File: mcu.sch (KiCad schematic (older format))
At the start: 45 parts

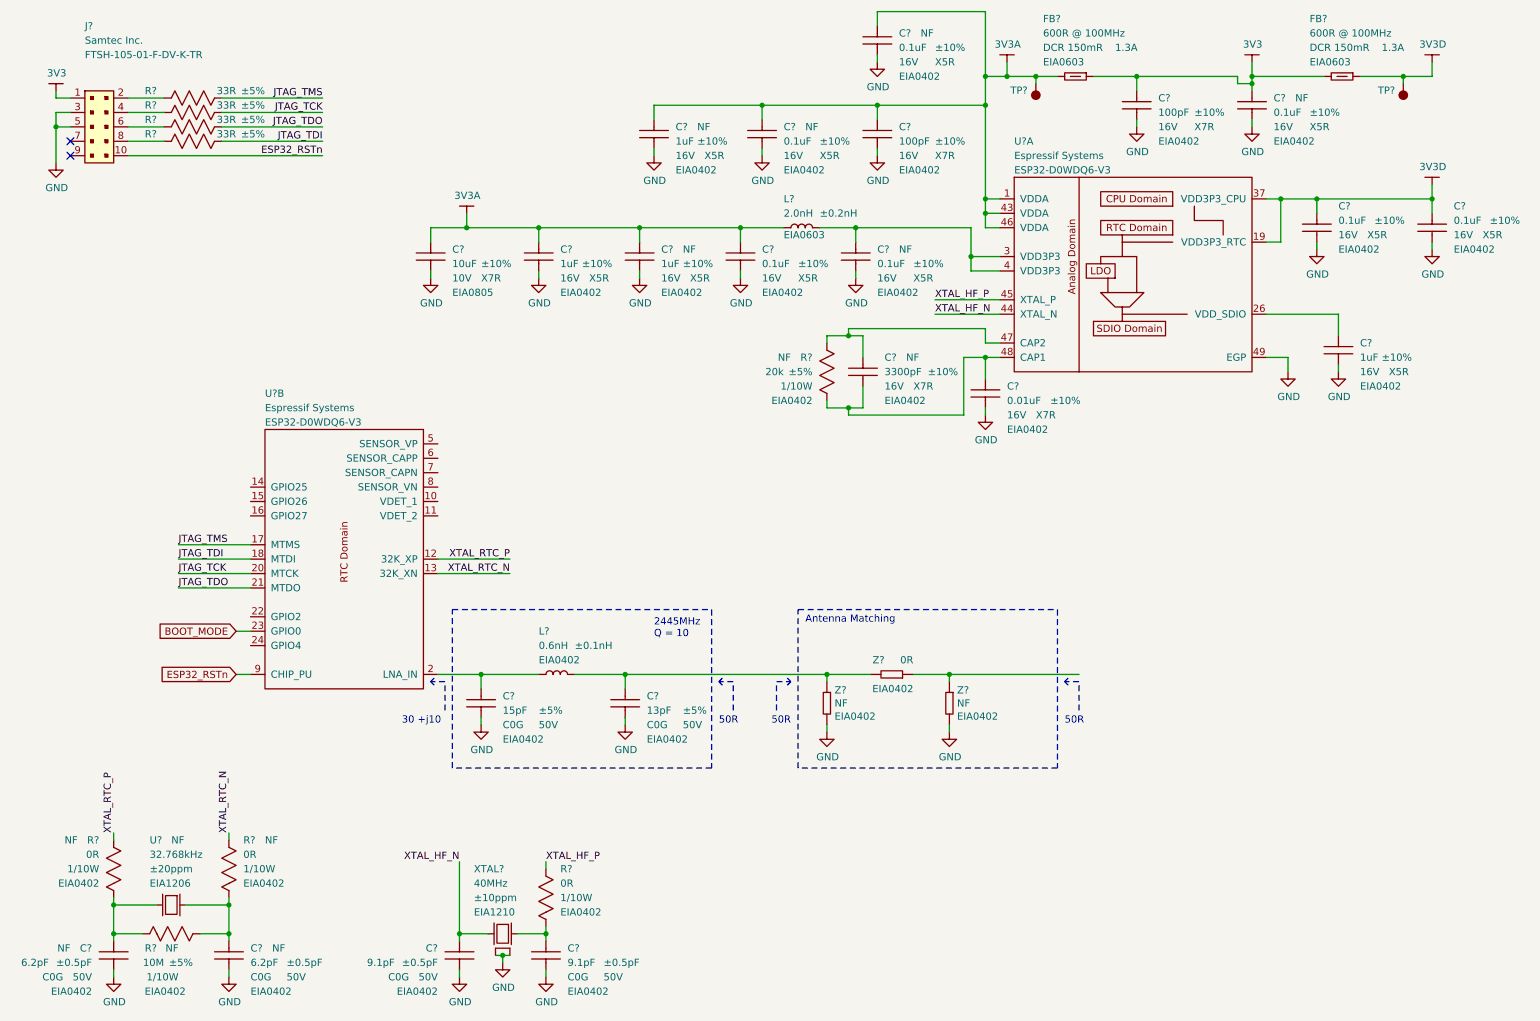
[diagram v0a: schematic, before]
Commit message: Bring out on headers all unused ESP32 pins.
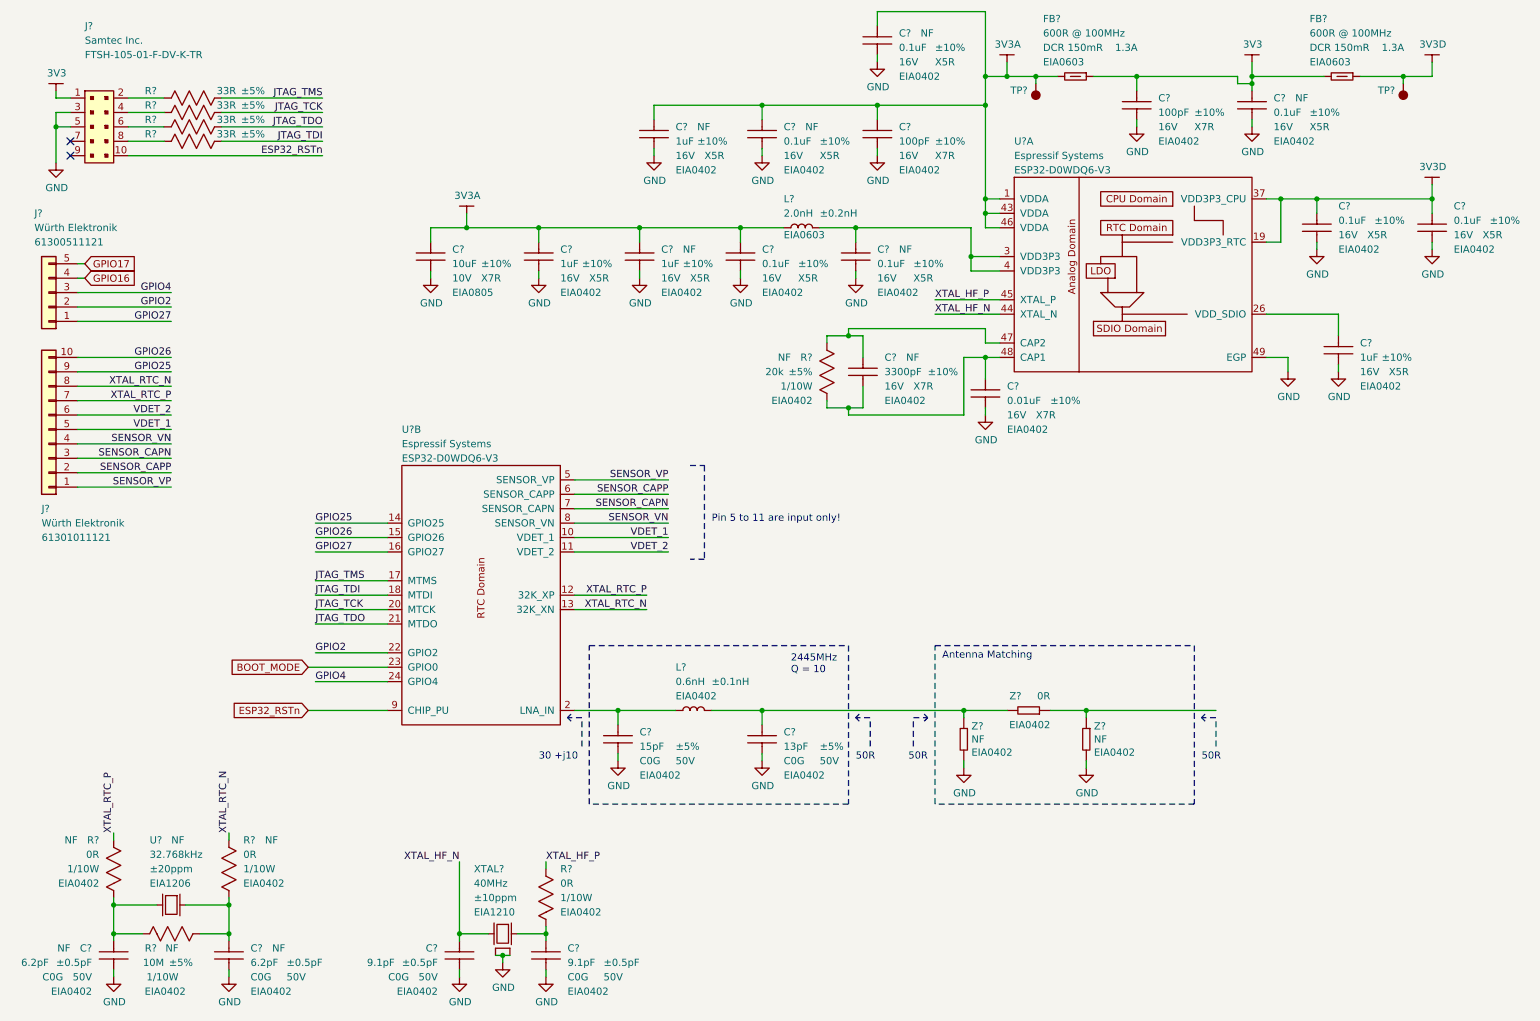
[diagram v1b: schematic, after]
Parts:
- added J?: WE-61301011121, footprints:WE-61301011121_HDRV10W64P254_10X1_2540X254X884N, symbol gz_Rectangular-Connectors-Headers-Male-Pins:WE-61301011121
- added J?: WE-61300511121, footprints:WE-61300511121_HDRV5W79P254_5X1_1270X254H854, symbol gz_Rectangular-Connectors-Headers-Male-Pins:WE-61300511121
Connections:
- net XTAL_RTC_N: now also J?.8 (Pin_8)
- net XTAL_RTC_P: now also J?.7 (Pin_7)
- net VDET_1: now reaches U?.10 (VDET_1)
- net VDET_1: now also J?.5 (Pin_5)
- net VDET_2: now reaches U?.11 (VDET_2)
- net VDET_2: now also J?.6 (Pin_6)
- net GPIO25: now reaches U?.14 (GPIO25)
- net GPIO25: now also J?.9 (Pin_9)
- net GPIO26: now reaches U?.15 (GPIO26)
- net GPIO26: now also J?.10 (Pin_10)
- net GPIO27: now reaches U?.16 (GPIO27)
- net GPIO27: now also J?.1 (Pin_1)
- net GPIO2: now reaches U?.22 (GPIO2)
- net GPIO2: now also J?.2 (Pin_2)
- net GPIO4: now reaches U?.24 (GPIO4)
- net GPIO4: now also J?.3 (Pin_3)
- net SENSOR_VP: now reaches U?.5 (SENSOR_VP)
- net SENSOR_VP: now also J?.1 (Pin_1)
- net SENSOR_CAPP: now reaches U?.6 (SENSOR_CAPP)
- net SENSOR_CAPP: now also J?.2 (Pin_2)
- net SENSOR_CAPN: now reaches U?.7 (SENSOR_CAPN)
- net SENSOR_CAPN: now also J?.3 (Pin_3)
- net SENSOR_VN: now reaches U?.8 (SENSOR_VN)
- net SENSOR_VN: now also J?.4 (Pin_4)
- new net GPIO16: J?.4 (Pin_4)
- new net GPIO17: J?.5 (Pin_5)
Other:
- note added: "Pin 5 to 11 are input only!"
- moved on the sheet: C?, L?, U?B, Z?

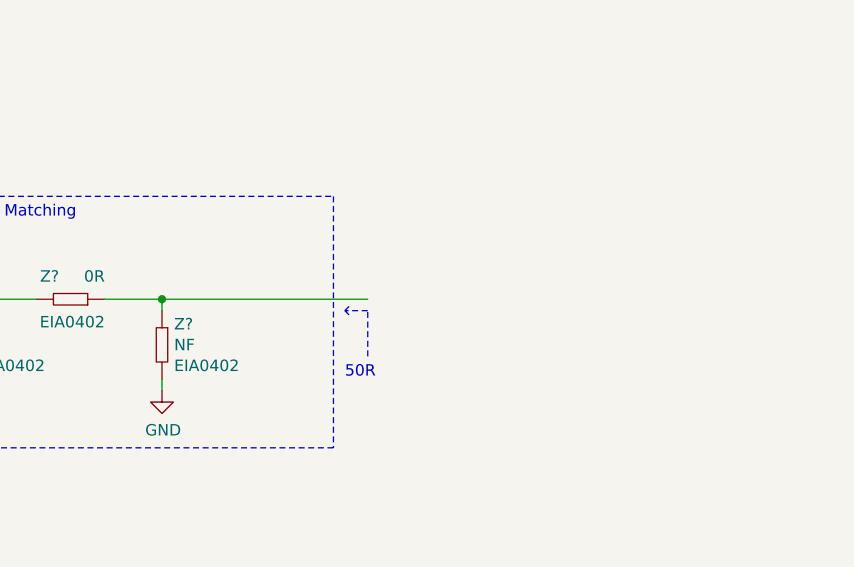
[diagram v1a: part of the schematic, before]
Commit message: Add antenna.
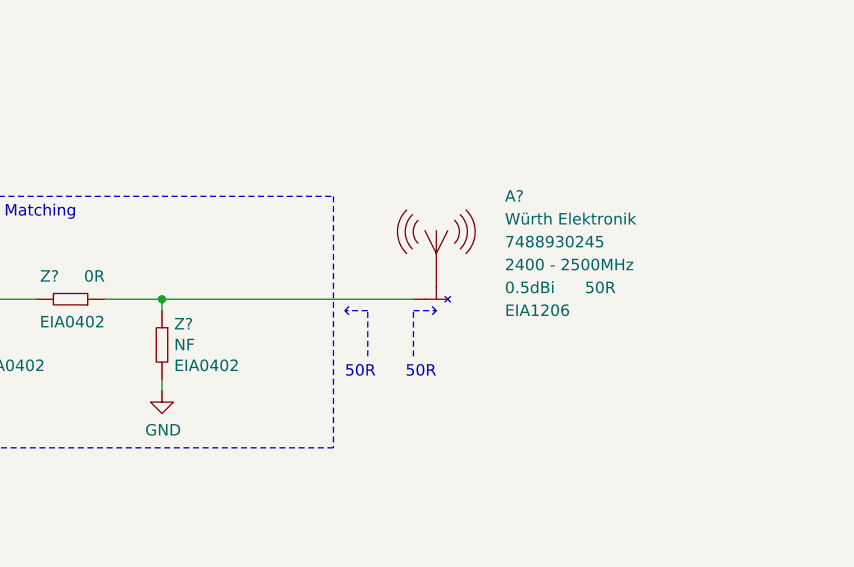
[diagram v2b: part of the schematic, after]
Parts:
- added A?: WE-7488930245, footprints:WE-7488930245_ANTC320X160X140L50N, symbol gz_RF-Antennas:WE-7488930245
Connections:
- net at Z?.1, Z?.1: now also A?.1
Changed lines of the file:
@@
 Wire Notes Line style solid
 	8900 5550 8925 5575
-Wire Wire Line
-	8100 5500 9000 5500
 Connection ~ 8100 5500
 Wire Wire Line
@@
 	1    0    0    1
 $EndComp
+$Comp
+L gz_RF-Antennas:WE-7488930245 A?
+U 1 1 60620A37
+P 9200 5500
+F 0 "A?" H 9600 5950 50  0000 L CNN
+F 1 "WE-7488930245" H 10000 6400 50  0001 L CNN
+F 2 "footprints:WE-7488930245_ANTC320X160X140L50N" H 10000 6500 50  0001 L CNN
+F 3 "${DATASHEETS}/WE-7488930245.pdf" H 10250 5650 50  0001 L CNN
+F 4 "Digikey" H 10000 6300 50  0001 L CNN "Vendor"
+F 5 "732-1843-1-ND" H 10350 6300 50  0001 L CNN "Vendor_PN"
+F 6 "Würth Elektronik" H 9600 5850 50  0000 L CNN "Manufacturer"
+F 7 "7488930245" H 9600 5750 50  0000 L CNN "MPN"
+F 8 "RF/IF and RFID" H 10000 6200 50  0001 L CNN "Category"
+F 9 "RF Antennas" H 10000 6100 50  0001 L CNN "Family"
+F 10 "2400 - 2500MHz" H 9600 5650 50  0000 L CNN "Frequency"
+F 11 "0.5dBi" H 9600 5550 50  0000 L CNN "Peak Gain"
+F 12 "50R" H 9950 5550 50  0000 L CNN "Impedance"
+F 13 "Yes" H 9600 5350 50  0001 L CNN "Fit"
+F 14 "EIA1206" H 9600 5450 50  0000 L CNN "Package"
+	1    9200 5500
+	1    0    0    -1
+$EndComp
+Wire Wire Line
+	8100 5500 9200 5500
+Text Notes 9300 5850 2    50   ~ 0
+50R
+Wire Notes Line style solid
+	9200 5750 9200 5550
+Wire Notes Line style solid
+	9200 5550 9300 5550
+Wire Notes Line style solid
+	9300 5550 9275 5525
+Wire Notes Line style solid
+	9300 5550 9275 5575
 $EndSCHEMATC

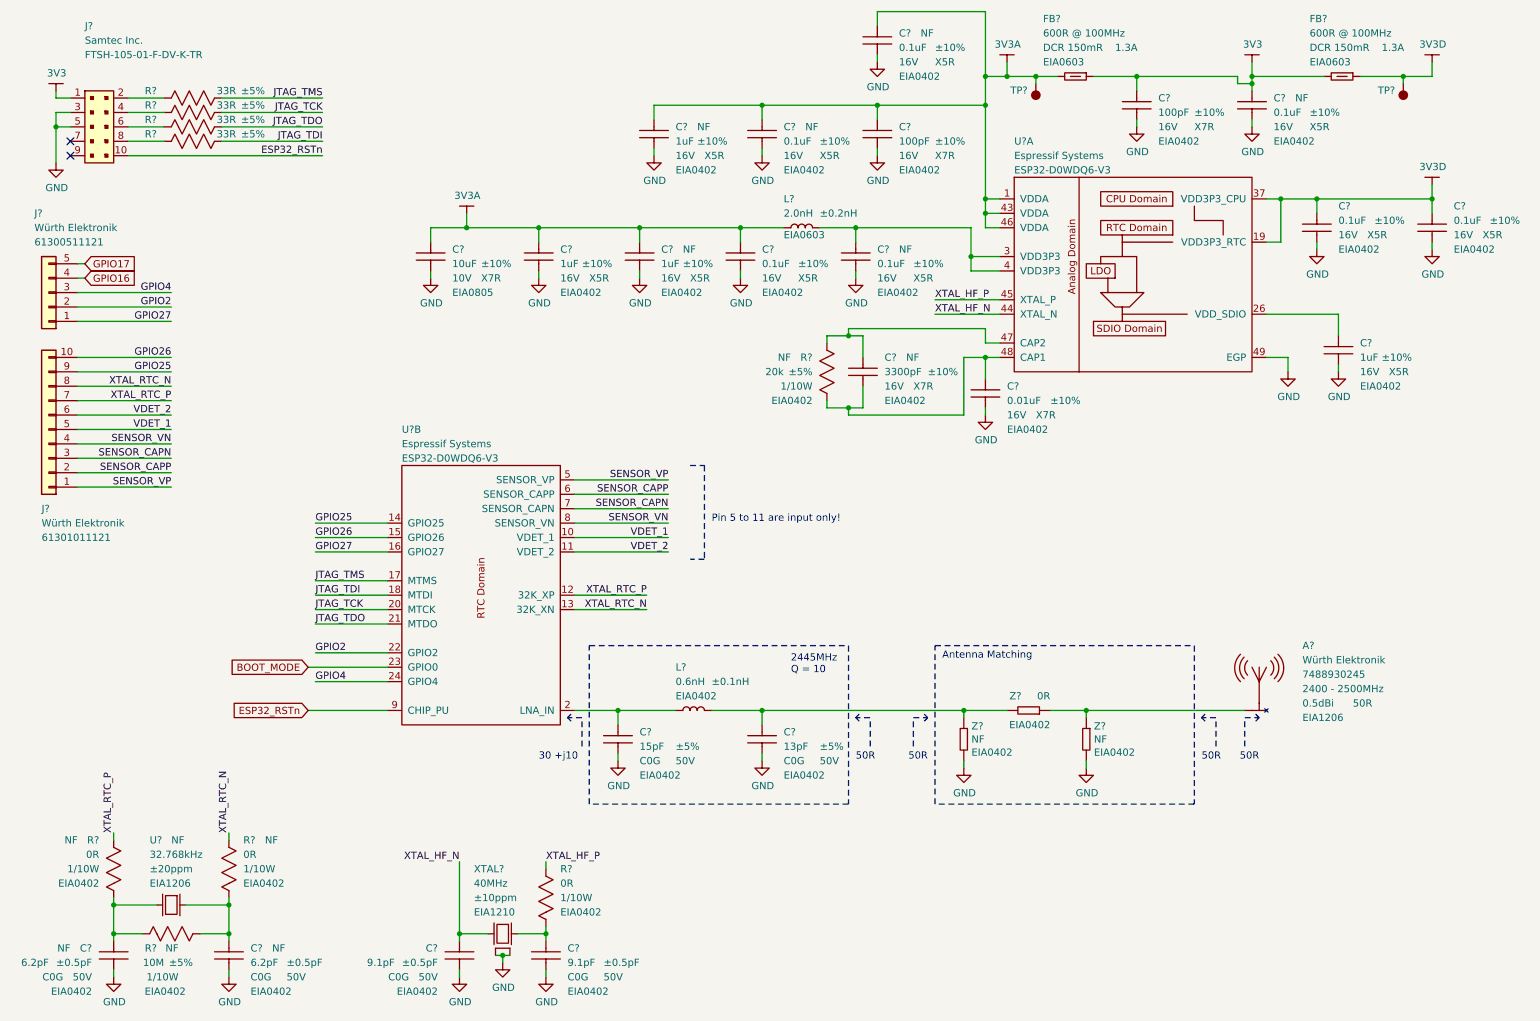
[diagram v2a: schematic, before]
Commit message: Annotate schematic.
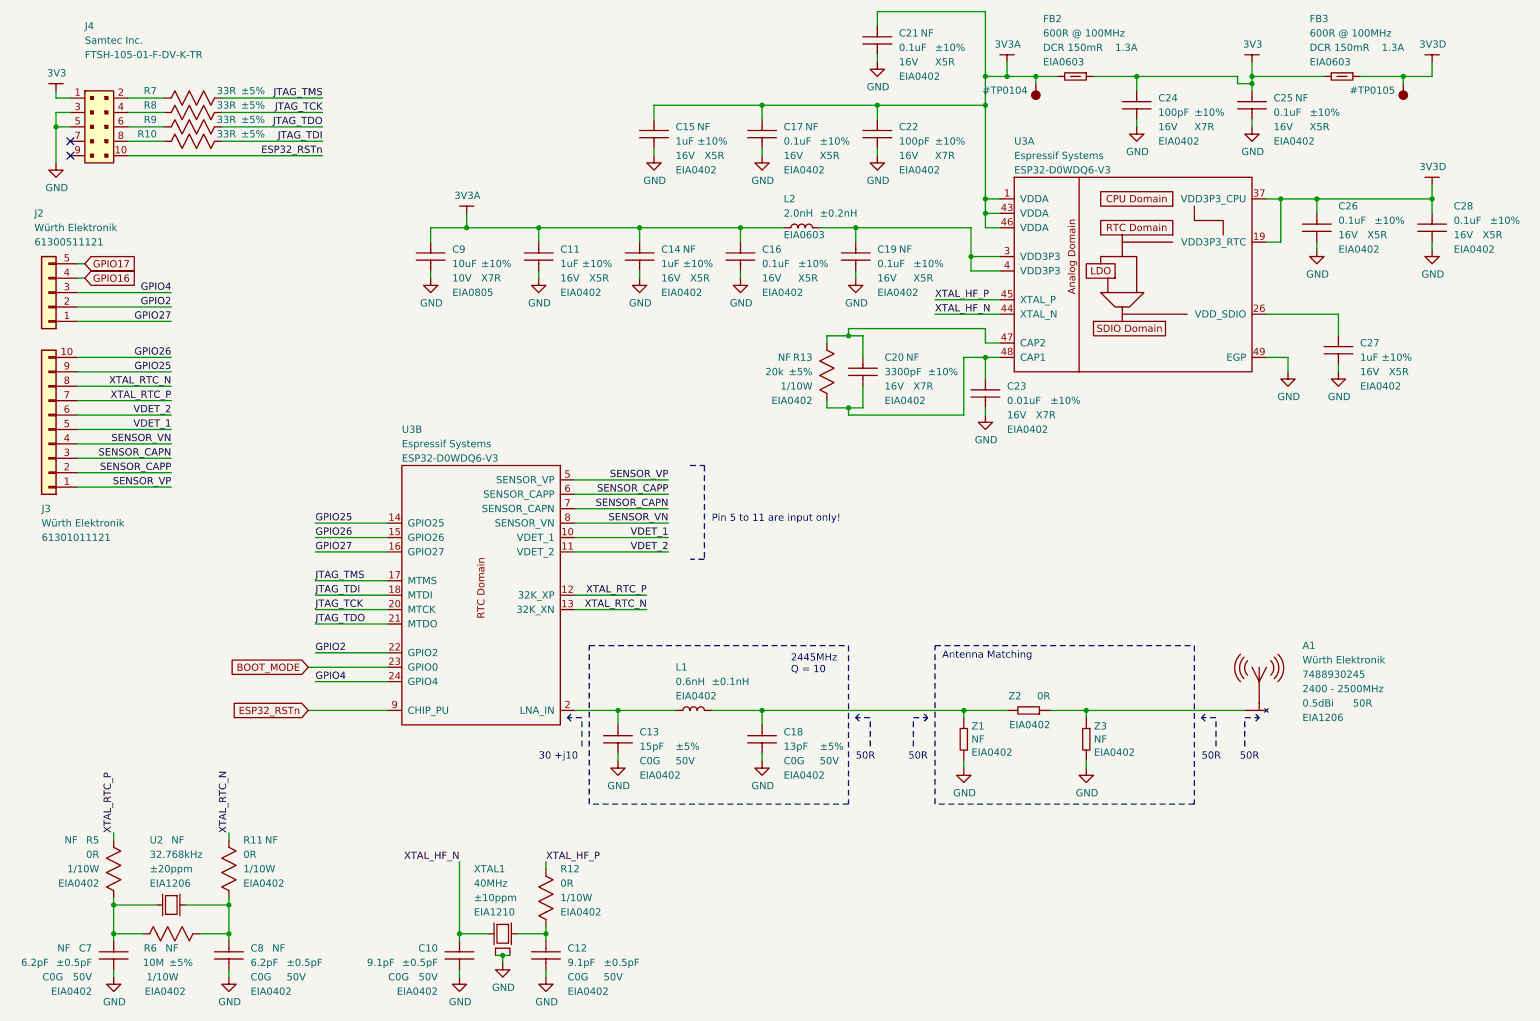
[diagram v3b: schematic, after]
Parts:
- removed TP? (x2): Test-Point-SMT, footprints_generic:TestPoint-SMT_C100, symbol gz_Test-Points:Test-Point-SMT
- gave numbers to parts that had none: 45

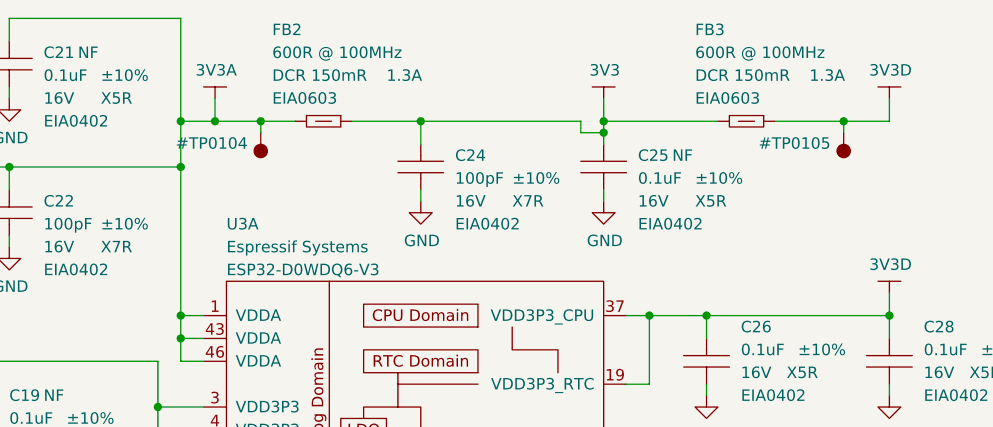
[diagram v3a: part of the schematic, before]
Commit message: Annotate test points.
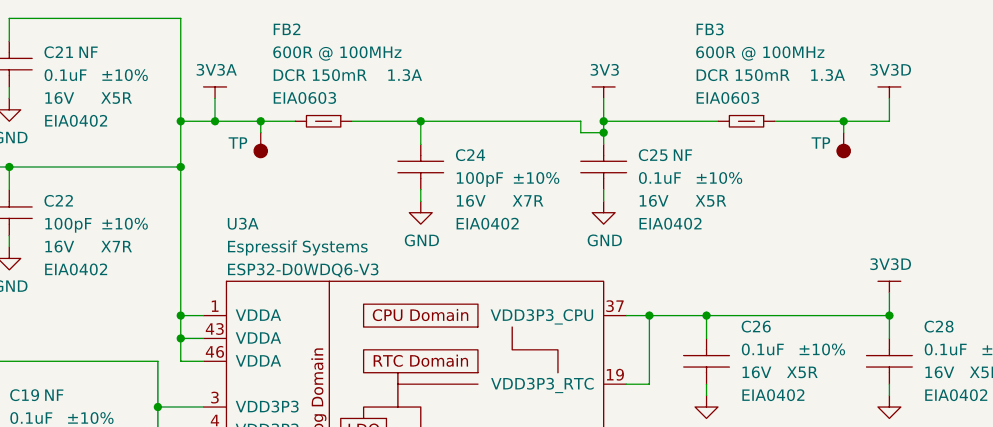
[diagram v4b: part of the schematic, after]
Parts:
- added TP (x2): Test-Point-SMT, footprints_generic:TestPoint-SMT_C100, symbol gz_Test-Points:Test-Point-SMT
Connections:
- net 3V3A: now also TP.1
- net 3V3D: now also TP.1
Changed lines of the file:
@@
 	3800 2150 3550 2150
 $Comp
-L gz_Test-Points:Test-Point-SMT #TP0104
+L gz_Test-Points:Test-Point-SMT TP
 U 1 1 60505B45
 P 7750 1150
-F 0 "#TP0104" H 7807 1197 50  0000 L CNN
+F 0 "TP" H 7807 1197 50  0000 L CNN
 F 1 "Test-Point-SMT" H 8050 1500 50  0001 L CNN
 F 2 "footprints_generic:TestPoint-SMT_C100" H 8050 1400 50  0001 L CNN
@@
 Connection ~ 10500 1950
 $Comp
-L gz_Test-Points:Test-Point-SMT #TP0105
+L gz_Test-Points:Test-Point-SMT TP
 U 1 1 605DAA4E
 P 10300 1150
-F 0 "#TP0105" H 10357 1197 50  0000 L CNN
+F 0 "TP" H 10357 1197 50  0000 L CNN
 F 1 "Test-Point-SMT" H 10600 1500 50  0001 L CNN
 F 2 "footprints_generic:TestPoint-SMT_C100" H 10600 1400 50  0001 L CNN
